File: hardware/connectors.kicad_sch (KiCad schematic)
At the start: 8 parts, among them J1 USB_B_Micro, J2 CON10, U2 NCP1117-3.3_SOT223

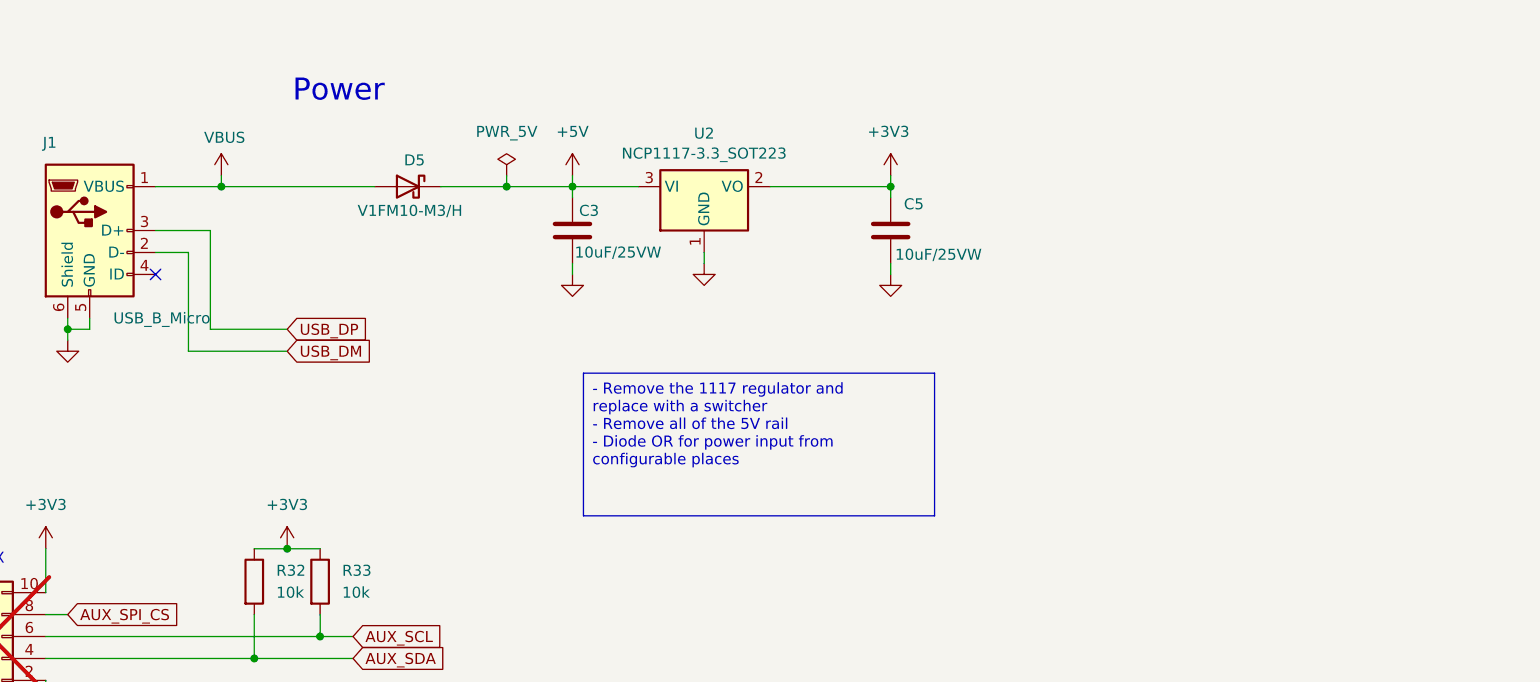
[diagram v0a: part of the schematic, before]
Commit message: Cleaned up share library Added switchmode 3v3 supply
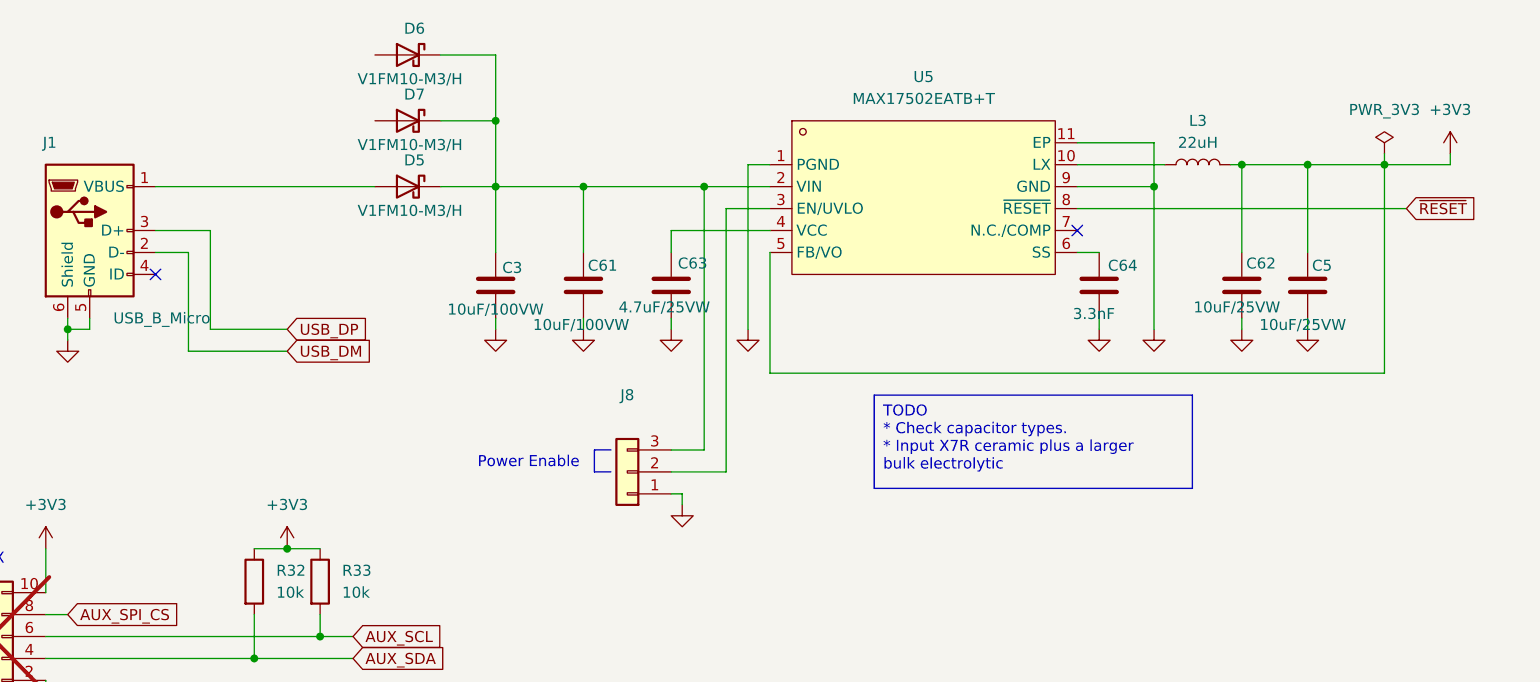
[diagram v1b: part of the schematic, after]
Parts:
- removed U2: NCP1117-3.3_SOT223, Package_TO_SOT_SMD:SOT-223-3_TabPin2, symbol Regulator_Linear:NCP1117-3.3_SOT223
- added C61: 10uF/100VW, Capacitor_SMD:CP_Elec_6.3x7.7, symbol Device:C
- added C62: 10uF/25VW, Capacitor_SMD:C_0805_2012Metric, symbol Device:C
- added C63: 4.7uF/25VW, Capacitor_SMD:C_0805_2012Metric, symbol Device:C
- added C64: 3.3nF, Capacitor_SMD:C_0603_1608Metric, symbol Device:C
- added D6, D7: V1FM10-M3/H, Diode_SMD:D_SMF, symbol Device:D_Schottky
- added J8: Conn_01x03, symbol Connector_Generic:Conn_01x03
- added L3: 22uH, BidirectionalSupply:IND-SMD_L4.0-W4.0_SLW4010S, symbol Device:L
- added U5: MAX17502EATB+T, BidirectionalSupply:DFN-10_L3.0-W2.0-P0.50-BL-EP, symbol BidirectionalSupply:MAX17502FATB+T
- C3: value 10uF/25VW -> 10uF/100VW; footprint Capacitor_SMD:C_0805_2012Metric -> Capacitor_SMD:CP_Elec_6.3x7.7; JLCPCB C15850 -> C19077968
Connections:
- net +3V3: now also C62.1, L3.2, U5.5 (FB/VO)
- net GND: now also C61.2, C62.2, C63.2, C64.2, J8.1 (Pin_1), U5.1 (PGND), U5.11 (EP), U5.9 (GND)
- net +5V: no longer names the net of C3.1, D5.1 (K)
- net +5V: now also C61.1, D6.1 (K), D7.1 (K), J8.3 (Pin_3), U5.2 (VIN)
- net VBUS: no longer names the net of D5.2 (A), J1.1 (VBUS)
- new net: C63.1, U5.4 (VCC)
- new net: L3.1, U5.10 (LX)
- new net: J8.2 (Pin_2), U5.3 (EN/UVLO)
- new net: C64.1, U5.6 (SS)
- new net ~{RESET}: U5.8 (~{RESET})
- no-connect marks 1 -> 2
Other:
- note added: "Power Enable"
- note removed: "Power"

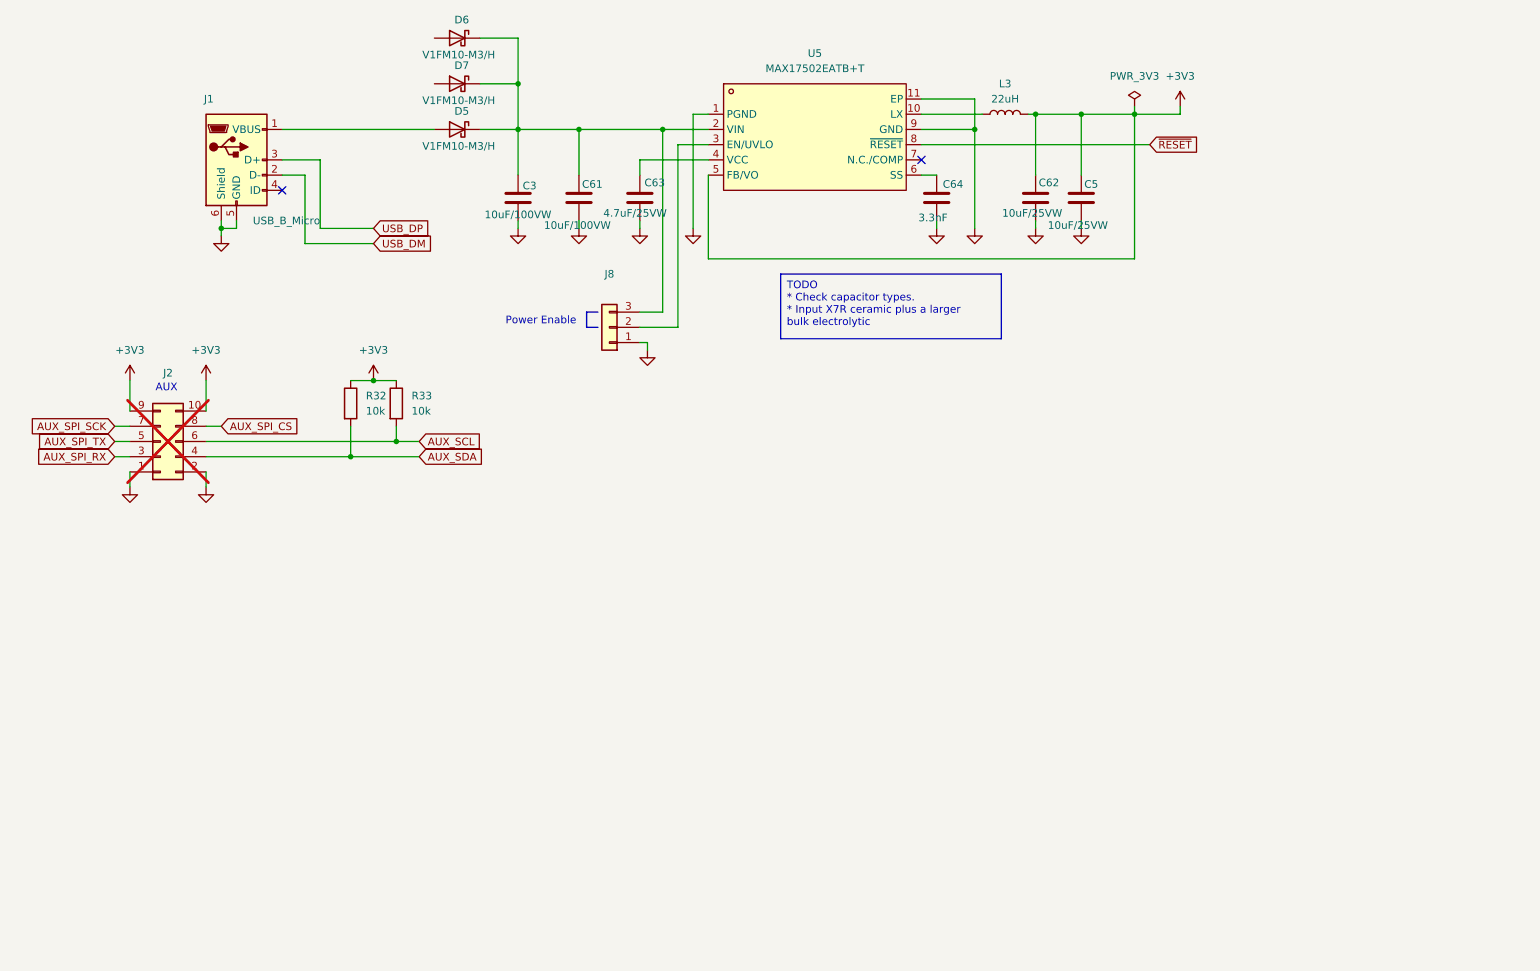
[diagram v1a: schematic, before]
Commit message: Schematic is now mostly complete. Will review and then move onto the PCB layout
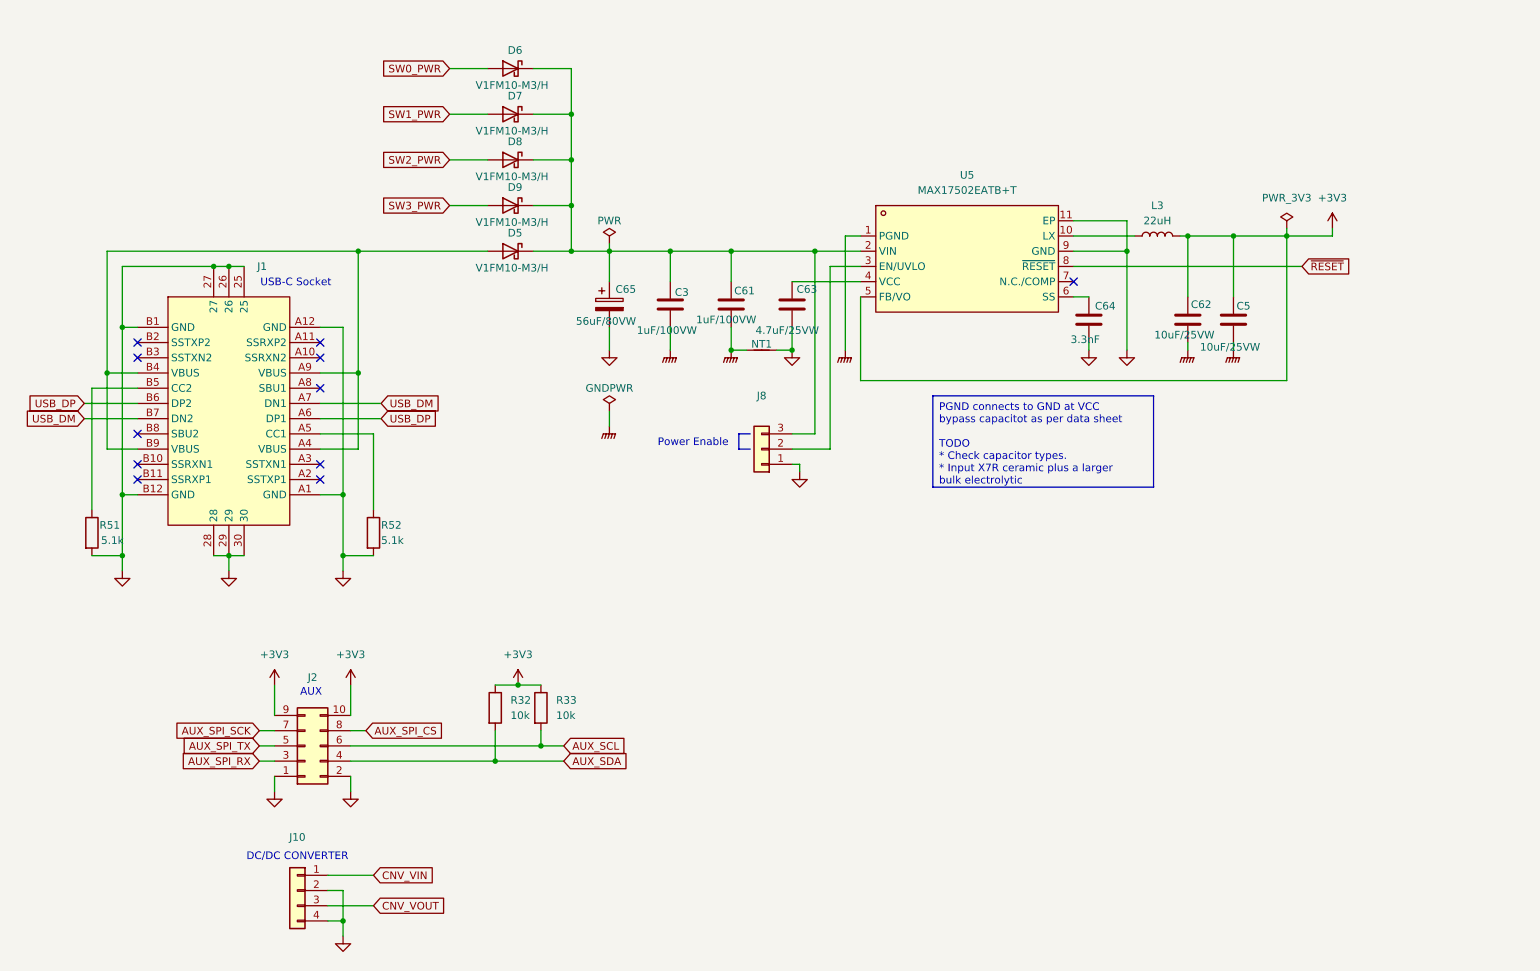
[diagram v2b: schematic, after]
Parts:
- removed J1: USB_B_Micro, Connector_USB:USB_Micro-B_Amphenol_10103594-0001LF_Horizontal, symbol Connector:USB_B_Micro
- added C65: 56uF/80VW, Capacitor_SMD:CP_Elec_10x10.5, symbol Device:C_Polarized
- added D8, D9: V1FM10-M3/H, Diode_SMD:D_SMF, symbol Device:D_Schottky
- added J1: USB-309GC-B-SU, BidirectionalSupply:USB-C-SMD_USB-309GC-B-SU, symbol BidirectionalSupply:USB-309GC-B-SU
- added J10: Conn_01x04, Connector_Phoenix_MSTB:PhoenixContact_MSTBVA_2,5_5-G-5,08_1x05_P5.08mm_Vertical, symbol Connector_Generic:Conn_01x04
- added NT1: NetTie_2, symbol Device:NetTie_2
- added R51, R52: 5.1k, Resistor_SMD:R_0603_1608Metric, symbol Device:R
- C3, C61: value 10uF/100VW -> 1uF/100VW; footprint Capacitor_SMD:CP_Elec_6.3x7.7 -> Capacitor_SMD:C_1206_3216Metric; JLCPCB C19077968 -> C13832
- J2: now fitted
- J8: footprint (none) -> Connector_PinHeader_2.54mm:PinHeader_1x03_P2.54mm_Vertical
- U5: LCSC Part C571005 -> C559500
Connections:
- net GND: now also C65.2, J1.25, J1.26, J1.27, J1.28, J1.29, J1.30, J1.A1 (GND), J1.A12 (GND), J1.B1 (GND), J1.B12 (GND), J10.2 (Pin_2), J10.4 (Pin_4), NT1.2, R51.2, R52.2; no longer C3.2, C5.2, C61.2, C62.2, U5.1 (PGND)
- net USB_DM: now also J1.A7 (DN1), J1.B7 (DN2)
- net USB_DP: now also J1.A6 (DP1), J1.B6 (DP2)
- net at D5.2 (A): now also J1.A4 (VBUS), J1.A9 (VBUS), J1.B4 (VBUS), J1.B9 (VBUS)
- net at C3.1, C61.1, D5.1 (K)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: now also C65.1, D8.1 (K), D9.1 (K)
- net SW1_PWR: now reaches D7.2 (A)
- net SW0_PWR: now reaches D6.2 (A)
- new net: J1.B5 (CC2), R51.1
- new net: J1.A5 (CC1), R52.1
- new net CNV_VIN: J10.1 (Pin_1)
- new net CNV_VOUT: J10.3 (Pin_3)
- new net GNDPWR: C3.2, C5.2, C61.2, C62.2, NT1.1, U5.1 (PGND)
- new net SW2_PWR: D8.2 (A)
- new net SW3_PWR: D9.2 (A)
- no-connect marks 2 -> 11
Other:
- note added: "DC/DC CONVERTER"
- note added: "USB-C Socket"
- moved on the sheet: C3, C5, C61, C62, C63, C64, D5, D6, D7, J8, L3, R32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

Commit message: Checked all DC/DC converter capacitors Some part substitution to preference in stock items
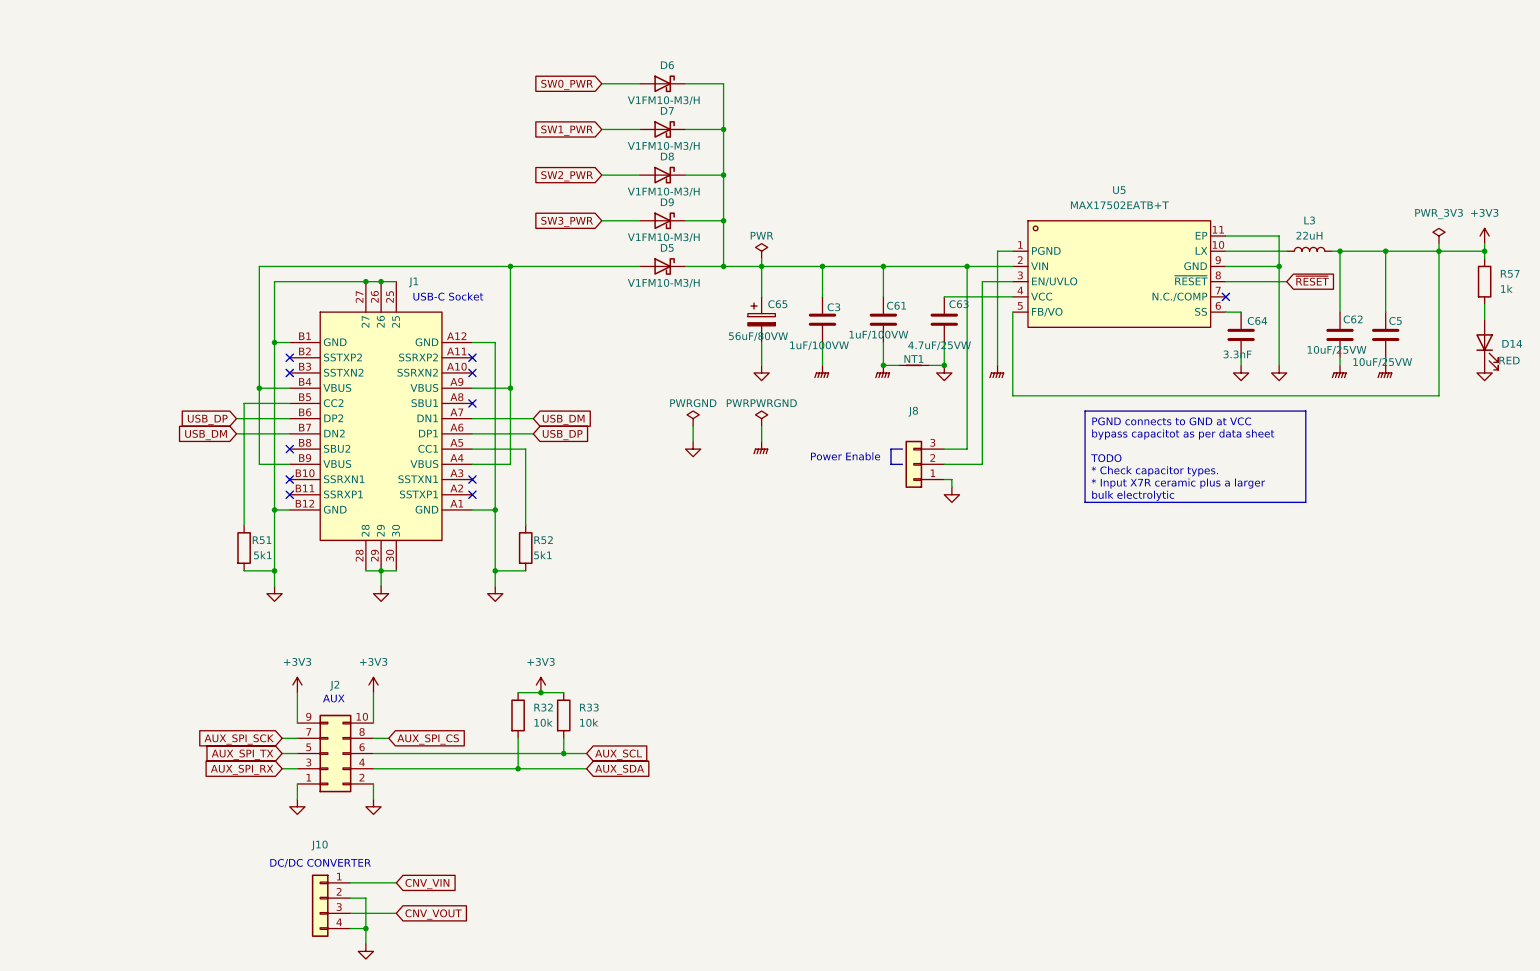
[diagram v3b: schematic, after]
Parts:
- added D14: RED, LED_SMD:LED_0603_1608Metric, symbol Device:LED
- added R57: 1k, Resistor_SMD:R_0603_1608Metric, symbol Device:R
- J10: Mouser (none) -> 651-1755752
- R51, R52: value 5.1k -> 5k1
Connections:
- net +3V3: now also R57.1
- net GND: now also D14.1 (K)
- new net: D14.2 (A), R57.2
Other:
- moved on the sheet: C3, C5, C61, C62, C63, C64, C65, D5, D6, D7, D8, D9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

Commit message: All components placed on board and most 3D shapes are present
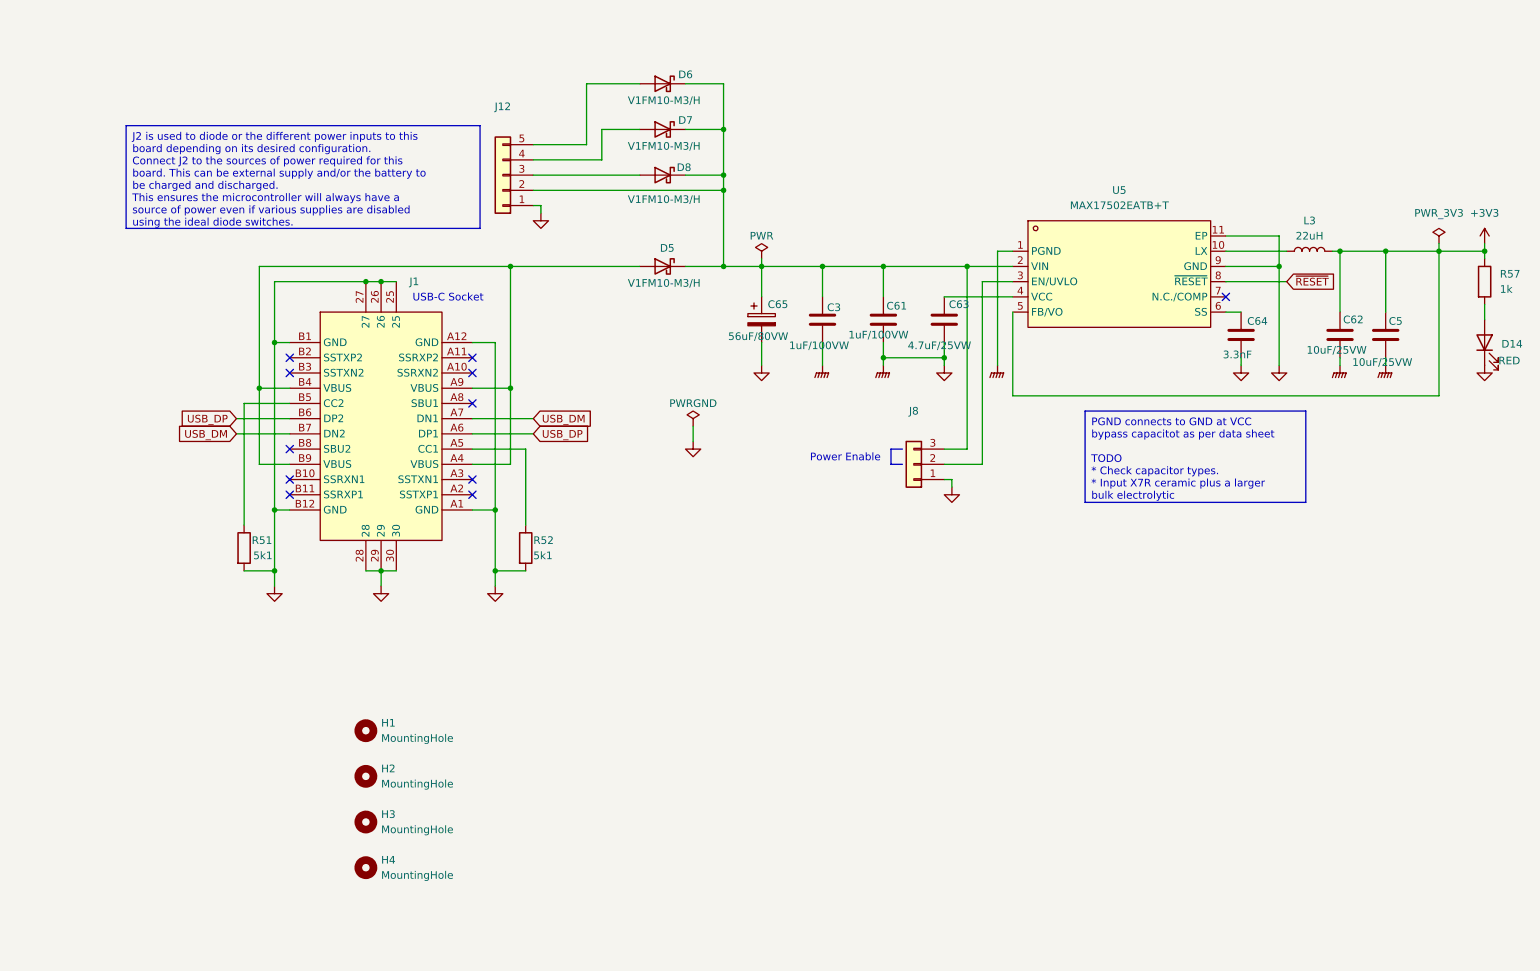
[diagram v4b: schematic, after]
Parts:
- removed D9: V1FM10-M3/H, Diode_SMD:D_SMF, symbol Device:D_Schottky
- removed J10: Conn_01x04, Connector_Phoenix_MSTB:PhoenixContact_MSTBVA_2,5_5-G-5,08_1x05_P5.08mm_Vertical, symbol Connector_Generic:Conn_01x04
- removed J2: CON10, Connector_PinHeader_2.54mm:PinHeader_2x05_P2.54mm_Vertical, symbol Connector_Generic:Conn_02x05_Odd_Even
- removed NT1: NetTie_2, symbol Device:NetTie_2
- removed R32, R33: 10k, Resistor_SMD:R_0603_1608Metric, symbol Device:R
- added H1, H2, H3, H4: MountingHole, MountingHole:MountingHole_3.2mm_M3_Pad, symbol Mechanical:MountingHole
- added J12: Conn_01x05, Connector_Phoenix_MSTB:PhoenixContact_MSTBVA_2,5_5-G-5,08_1x05_P5.08mm_Vertical, symbol Connector_Generic:Conn_01x05
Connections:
- net GNDPWR is gone; now on net GND: C3.2, C5.2, C61.2, C62.2, U5.1 (PGND)
- net GND: now also J12.1 (Pin_1)
- net at C3.1, C61.1, C65.1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: now also J12.2 (Pin_2)
- net SW0_PWR: no longer names the net of D6.2 (A)
- net SW0_PWR: now also J12.5 (Pin_5)
- net SW1_PWR: no longer names the net of D7.2 (A)
- net SW1_PWR: now also J12.4 (Pin_4)
- net SW2_PWR: no longer names the net of D8.2 (A)
- net SW2_PWR: now also J12.3 (Pin_3)
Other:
- note removed: "AUX"
- note removed: "DC/DC CONVERTER"

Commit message: Added summary page Added prototyping area to PCB
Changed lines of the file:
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@@
 		)
 	)
-	(text_box "PGND connects to GND at VCC bypass capacitot as per data sheet\n\nTODO\n* Check capacitor types. \n* Input X7R ceramic plus a larger bulk electrolytic"
+	(text_box "PGND connects to GND at VCC bypass capacitor as per data sheet\n"
 		(exclude_from_sim no)
 		(at 189.865 85.09 0)
-		(size 36.83 15.24)
+		(size 36.83 5.715)
 		(stroke
 			(width 0)
